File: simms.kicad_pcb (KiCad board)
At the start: 2 copper layers, 88.8 x 15 mm, 12 parts, among them J1 Conn_01x30, U1 DRAM_HY514400_1Mx4bit, U2 DRAM_HY514400_1Mx4bit, U3 DRAM_TMS4C1024_1Mx1bit

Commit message: connect CA9
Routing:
- net /A9: track 83.4 -> 80.6 mm
- net /CA9: track 8.15 -> 10.7 mm
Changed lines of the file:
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@@
-	)
-	(segment
-		(start 144.8 81.2)
-		(end 143.0485 81.2)
-		(width 0.25)
-		(layer "F.Cu")
-		(net 18)
 	)
 	(segment
 		(start 131.856 84.544)
 		(end 131.856 85.688)
-		(width 0.25)
-		(layer "F.Cu")
-		(net 18)
-	)
-	(segment
-		(start 143.0485 81.2)
-		(end 142.3 81.9485)
 		(width 0.25)
 		(layer "F.Cu")
@@
 	)
 	(segment
-		(start 142.8 83.2)
-		(end 144.8 83.2)
+		(start 143.7 82.3)
+		(end 141.371 84.629)
 		(width 0.25)
 		(layer "F.Cu")
@@
 	)
 	(segment
-		(start 140.740827 88.5)
+		(start 141.371 84.629)
+		(end 141.371 87.129)
+		(width 0.25)
+		(layer "F.Cu")
+		(net 31)
+	)
+	(segment
+		(start 141.371 87.129)
 		(end 140.740827 87.759173)
 		(width 0.25)
@@
 	)
 	(segment
-		(start 141.371 84.629)
-		(end 142.8 83.2)
+		(start 140.740827 87.759173)
+		(end 140.740827 88.5)
 		(width 0.25)
 		(layer "F.Cu")
@@
 	)
 	(segment
-		(start 140.740827 87.759173)
-		(end 141.371 87.129)
-		(width 0.25)
-		(layer "F.Cu")
-		(net 31)
-	)
-	(segment
-		(start 141.371 87.129)
-		(end 141.371 84.629)
-		(width 0.25)
-		(layer "F.Cu")
+		(start 146.946 82.3)
+		(end 143.7 82.3)
+		(width 0.25)
+		(layer "F.Cu")

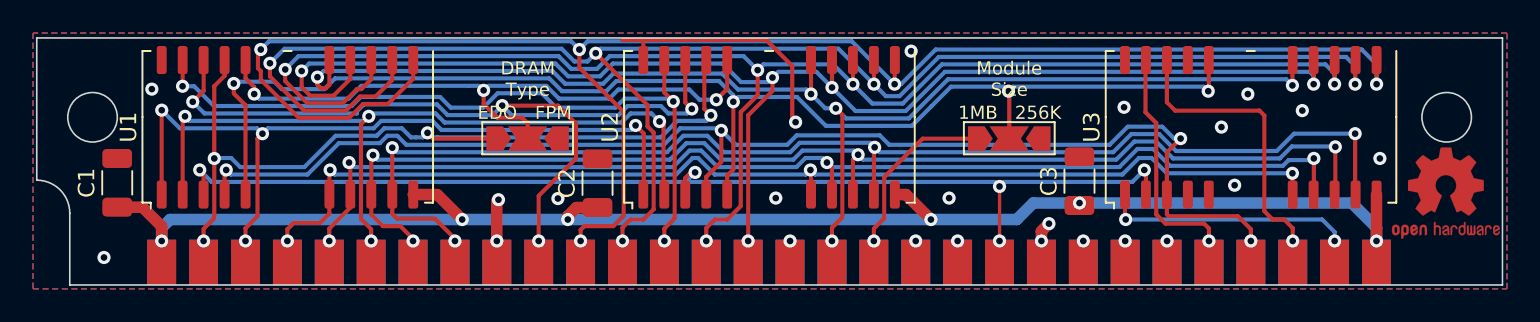
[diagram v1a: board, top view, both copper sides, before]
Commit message: fix incorrect data line connections; reroute entire board with thinner traces for neatness
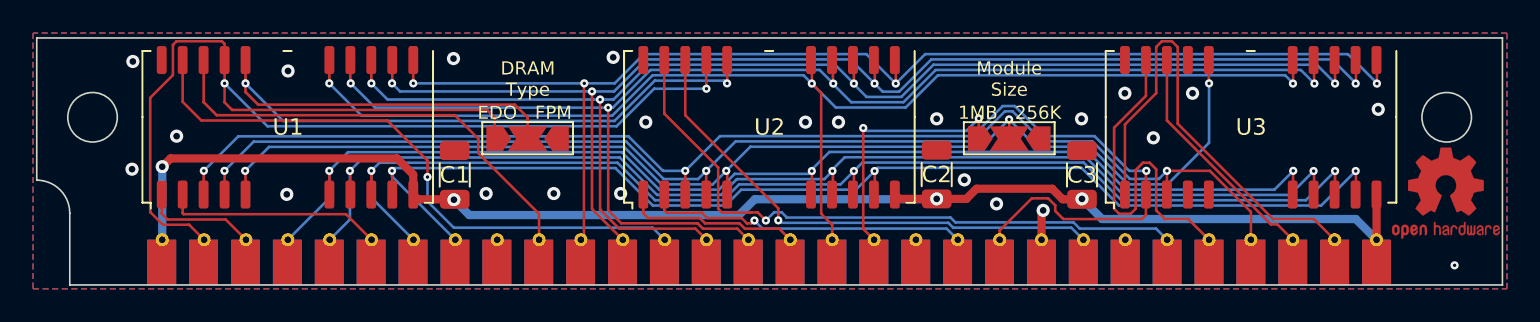
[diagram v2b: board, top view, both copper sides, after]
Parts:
- moved C2 20.6 mm to (144.6, 84.5)
- moved C1 20.5 mm to (115.3, 84.5)
- moved C3 0.40 mm to (153.3, 84.5)
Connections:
- U2 pad 1: /DQ0 -> /DQ4
- U2 pad 2: /DQ1 -> /DQ5
- U2 pad 24: /DQ2 -> /DQ6
- U2 pad 25: /DQ3 -> /DQ7
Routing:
- net /DQ0: track 46.4 -> 6.92 mm, vias 4 -> 0
- net /DQ7: track 0.00 -> 38.8 mm
- net /DQ1: track 47.1 -> 13.2 mm, vias 4 -> 0
- net /DQ6: track 0.00 -> 31.0 mm
- net /A4: track 103.8 -> 75.2 mm, vias 5 -> 4
- net /DQ2: track 51.0 -> 27.8 mm, vias 4 -> 0
- net /A5: track 98.3 -> 75.6 mm, vias 5 -> 4
- net /~{CAS}: track 52.2 -> 72.5 mm, vias 4 -> 2
- net /DQ5: track 0.00 -> 19.6 mm
- net GND: track 19.7 -> 1.82 mm, vias 17 -> 23
- net /~{OE}: track 39.3 -> 53.6 mm, vias 3 -> 2
- net /DP: track 15.0 -> 28.4 mm, vias 2 -> 0
- net /~{WE}: track 67.1 -> 78.7 mm, vias 5 -> 3
- net /A6: track 91.1 -> 80.0 mm, vias 5 -> 4
- net /DQ4: track 0.00 -> 10.7 mm, vias 1 -> 0
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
